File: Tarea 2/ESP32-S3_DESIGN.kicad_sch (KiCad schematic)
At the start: 31 parts, among them U1 ESP32-S3, U2 W25Q128JVS, U3 ESP-PSRAM32, U4 AMS1117-3.3, Y1 Crystal_Small

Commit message: Diseño de ESP32-S3 en KiCAD
Esta es la primera fase del diseño de una ESP32-S3, Aquí estamos realizando los esquematicos para la placa que vamos a desarrollar.
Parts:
- added C19: 0.1uF, symbol Device:C_Small
- added L8: TBD, symbol Device:L_Small
- added R3, R4, R6, R7, R8: 0, symbol Device:R_Small_US
- C7: value 0.1uF -> 1uF
- R2: value R_Small_US -> 499
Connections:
- net GND: now also U1.57 (GND), C19.2
- net LNA_IN: now also U1.1 (LNA_IN/RF)
- net SPICLK: now also R6.1
- net SPICS0: now also U1.32 (SPICS0/GPIO29)
- net SPID: now also R8.1
- net SPIHD: now also R3.1
- net SPIQ: now also R7.1
- net SPIWP: now also R4.1
- net VDD: now also U1.55 (VDDA), U1.56 (VDDA)
- net VDD_SPI: now also U1.29 (VDD_SPI)
- net XTAL_N: now also U1.53 (XTAL_N)
- net XTAL_P: now also L8.1
- net at C18.1: now also U1.20 (VDD3P3_RTC)
- net at R2.1: now also U1.49 (U0TXD/PROG/GPIO43)
- net U0TXD: now reaches R2.2
- net GPIO5: now reaches U1.10 (GPIO5/ADC1_CH4)
- net GPIO6: now reaches U1.11 (GPIO6/ADC1_CH5)
- net GPIO7: now reaches U1.12 (GPIO7/ADC1_CH6)
- net GPIO8: now reaches U1.13 (GPIO8/ADC1_CH7)
- net GPIO9: now reaches U1.14 (GPIO9/ADC1_CH8)
- net GPIO10: now reaches U1.15 (GPIO10/ADC1_CH9)
- net GPIO11: now reaches U1.16 (GPIO11/ADC2_CH0)
- net GPIO12: now reaches U1.17 (GPIO12/ADC2_CH1)
- net GPIO13: now reaches U1.18 (GPIO13/ADC2_CH2)
- net GPIO14: now reaches U1.19 (GPIO14/ADC2_CH3)
- net GPIO19: now reaches U1.25 (GPIO19/USB_D-/ADC2_CH8)
- net GPIO20: now reaches U1.26 (GPIO20/USB_D+/ADC2_CH9)
- net SPICS1 - GPIO26: now reaches U1.28 (SPI_CS1/GPIO26)
- net at U1.30 (SPIHD/GPIO27): now also R3.2
- net at U1.31 (SPIWP/GPIO28): now also R4.2
- net at U1.33 (SPICLK/GPIO30): now also R6.2
- net at U1.34 (SPIQ/GPIO31): now also R7.2
- net at U1.35 (SPID/GPIO32): now also R8.2
- net GPIO33: now reaches U1.38 (GPIO33)
- net GPIO34: now reaches U1.39 (GPIO34)
- net CHIP_PU: now reaches U1.4 (CHIP_PU/RESET)
- net GPIO35: now reaches U1.40 (GPIO35)
- net GPIO36: now reaches U1.41 (GPIO36)
- net GPIO37: now reaches U1.42 (GPIO37)
- net GPIO39: now reaches U1.44 (MTCK/JTAG/GPIO39)
- net GPIO40: now reaches U1.45 (MTDO/JTAG/GPIO40)
- net at U1.46 (VDD3P3_CPU): now also C19.1
- net GPIO41: now reaches U1.47 (MTDI/JTAG/GPIO41)
- net GPIO42: now reaches U1.48 (MTMS/JTAG/GPIO42)
- net GPIO0: now reaches U1.5 (GPIO0/BOOT)
- net U0RXD: now reaches U1.50 (U0RXD/PROG/GPIO44)
- net at U1.54 (XTAL_P): now also L8.2
- net GPIO1: now reaches U1.6 (GPIO1/ADC1_CH0)
- net GPIO2: now reaches U1.7 (GPIO2/ADC1_CH1)
- net GPIO3: now reaches U1.8 (GPIO3/ADC1_CH2)
- net GPIO4: now reaches U1.9 (GPIO4/ADC1_CH3)
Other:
- moved on the sheet: C12, C15, C16, C17, C18, L7, U1

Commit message: Diseño de ESP32-S3 en KiCAD
Esta es la primera fase del diseño de una ESP32-S3, Aquí estamos realizando los esquematicos para la placa que vamos a desarrollar.
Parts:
- removed C1: 10uF, symbol Device:C_Small
- removed D1: ESD, symbol Device:D_Small
- added C12: 10uF, symbol Device:C_Small
- added C20, C21: 0.1uF, symbol Device:C_Small
- added D2: ESD, symbol Device:D_Small
- added J1: USB_C_Receptacle_USB2.0_14P, symbol Connector:USB_C_Receptacle_USB2.0_14P
- added R7, R8: 5.1k, symbol Device:R_Small_US
- added U5: CH340C, Package_SO:SOIC-16_3.9x9.9mm_P1.27mm, symbol Interface_USB:CH340C
- renumbered C2 to C1, C11 to C10, C16 to C11, C17 to C13, C6 to C14, C7 to C15, C18 to C16, C19 to C17, C14 to C18, C13 to C19, C4 to C2, C8 to C3, C5 to C4, C9 to C5, C3 to C6, C10 to C7, C12 to C8, C15 to C9, D2 to D1, L4 to L1, L5 to L2, L6 to L3, L7 to L4, L8 to L5, R3 to R1, R4 to R2, R6 to R3, R7 to R4, R8 to R5, R2 to R6, U4 to U1, U1 to U4
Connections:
- net GND: now also C12.2, C20.1, C21.1, D2.1 (K), J1.A1 (GND), J1.A12 (GND), J1.B1 (GND), J1.B12 (GND), J1.SH (SHIELD), R7.2, R8.2, U5.1 (GND)
- net U0RXD: now also U5.2 (TXD)
- net U0TXD: now also U5.3 (RXD)
- net VBUS: now also C12.1, D2.2 (A), J1.A4 (VBUS), J1.A9 (VBUS), J1.B4 (VBUS), J1.B9 (VBUS)
- net VDD: now also C20.2, C21.2, U5.16 (VCC), U5.4 (V3)
- new net: J1.B5 (CC2), R8.1
- new net: J1.A5 (CC1), R7.1
- new net D+: J1.A6 (D+), J1.B6 (D+), U5.5 (UD+)
- new net D-: J1.A7 (D-), J1.B7 (D-), U5.6 (UD-)
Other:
- moved on the sheet: AE1, C1, C10, C11, C13, C16, C17, C18, C19, C2, C3, C4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

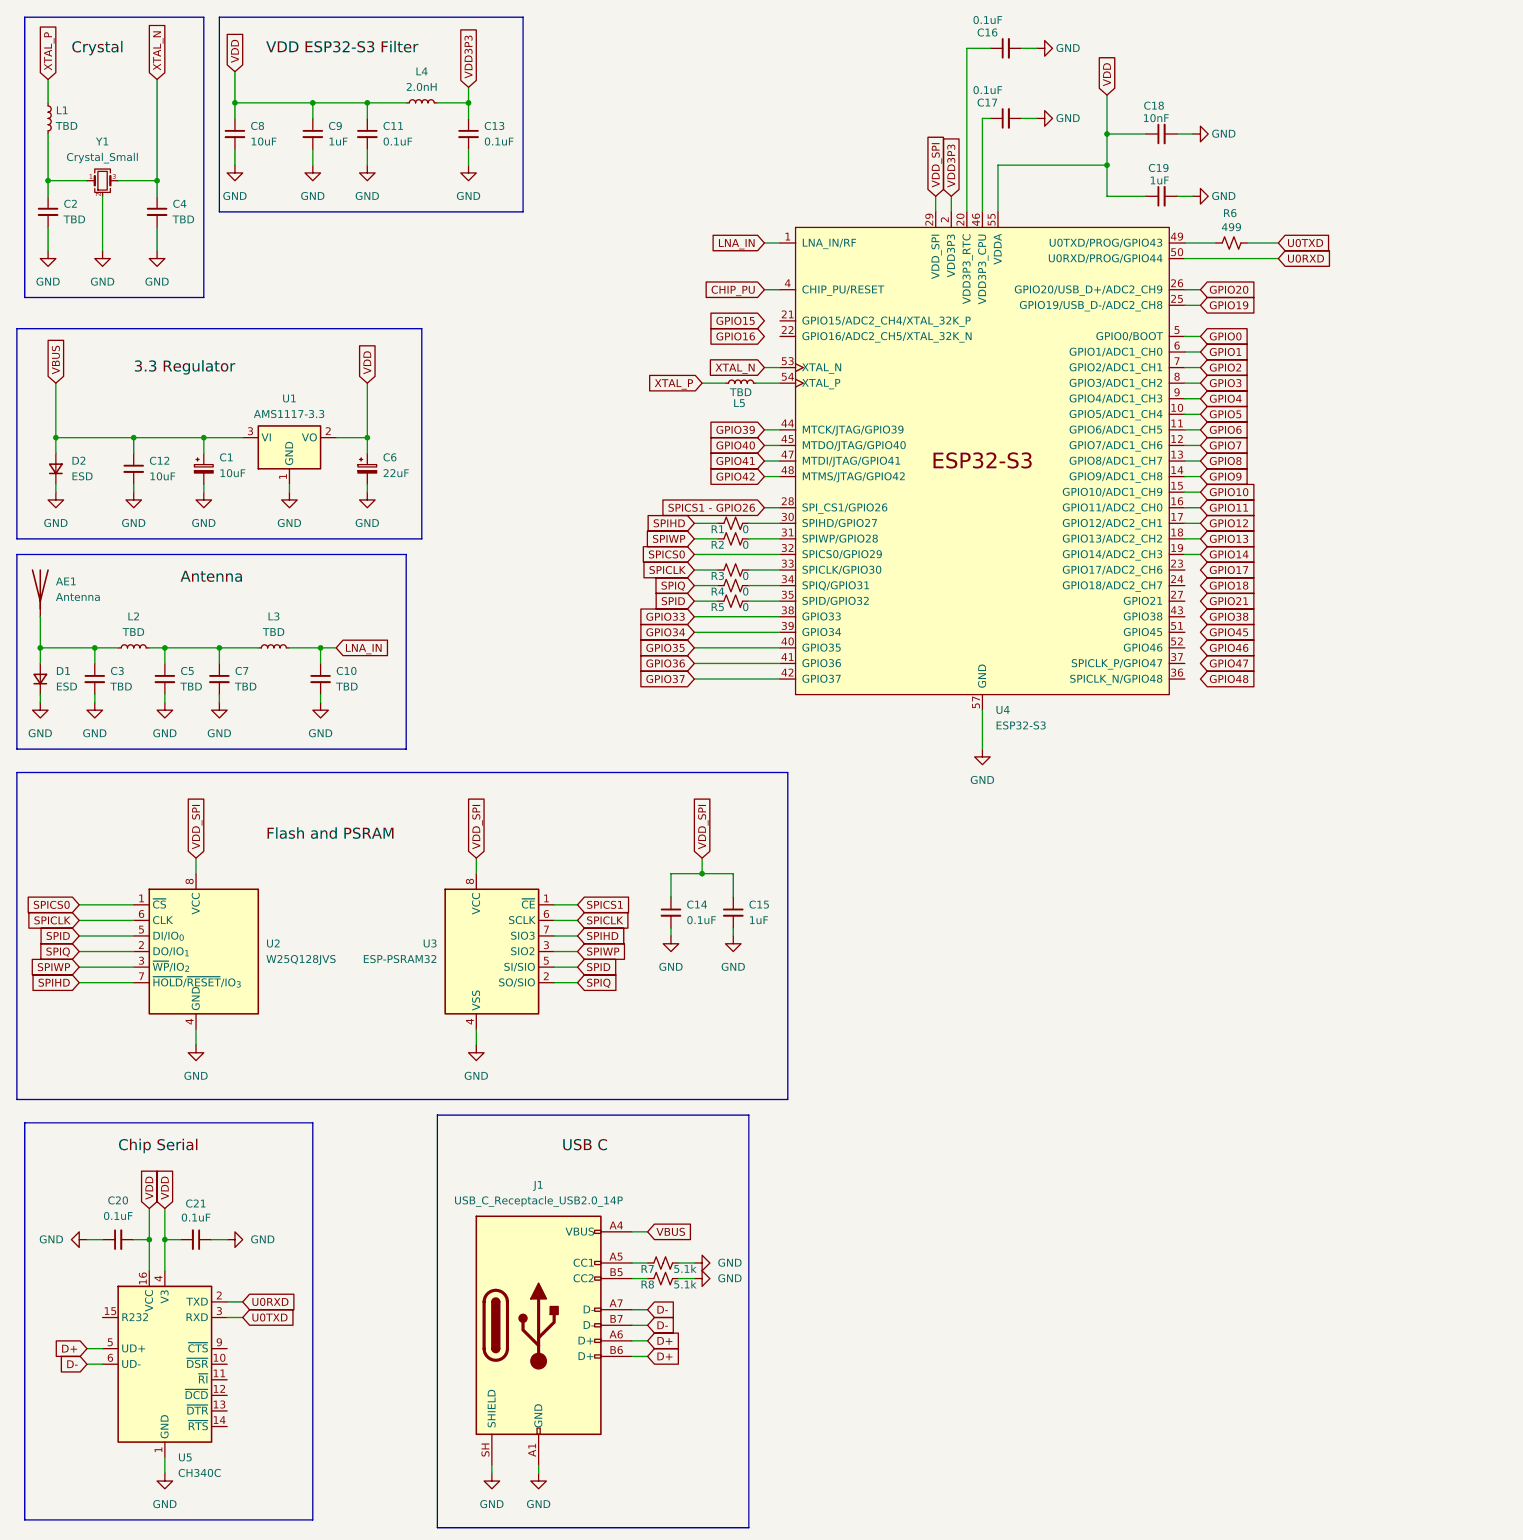
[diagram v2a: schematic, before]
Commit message: Diseño de ESP32-S3 en KiCAD
Esta es la primera fase del diseño de una ESP32-S3, Aquí estamos realizando los esquematicos de la parte del esp32 para la placa que vamos a desarrollar.
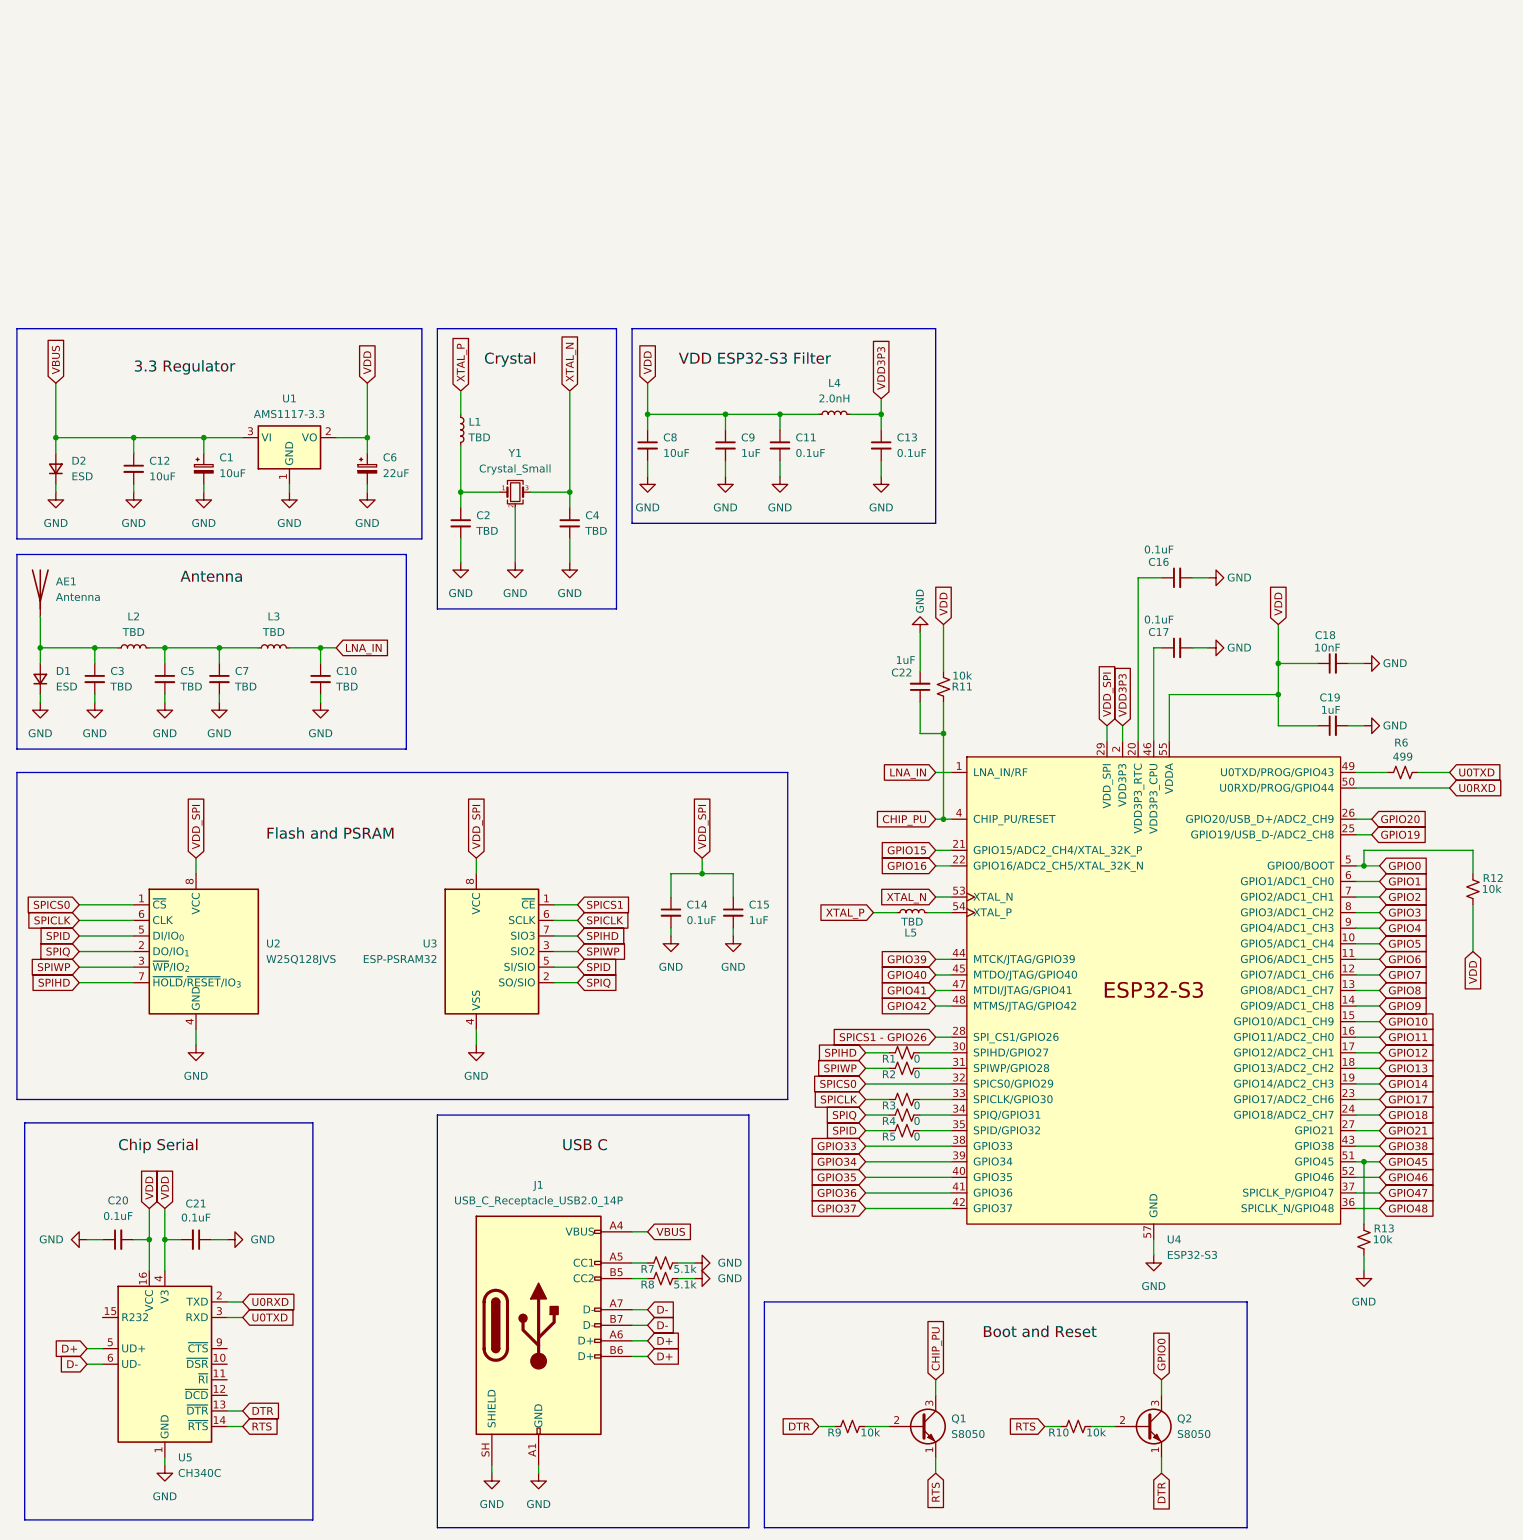
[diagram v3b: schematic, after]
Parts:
- added C22: 1uF, symbol Device:C_Small
- added Q1, Q2: S8050, Package_TO_SOT_THT:TO-92_Inline, symbol Transistor_BJT:S8050
- added R10, R11, R12, R13, R9: 10k, symbol Device:R_Small_US
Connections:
- net CHIP_PU: now also C22.1, Q1.3 (C), R11.1
- net GND: now also C22.2, R13.2
- net GPIO0: now also Q2.3 (C), R12.1
- net GPIO15: now also U4.21 (GPIO15/ADC2_CH4/XTAL_32K_P)
- net GPIO16: now also U4.22 (GPIO16/ADC2_CH5/XTAL_32K_N)
- net GPIO17: now also U4.23 (GPIO17/ADC2_CH6)
- net GPIO18: now also U4.24 (GPIO18/ADC2_CH7)
- net GPIO21: now also U4.27 (GPIO21)
- net GPIO38: now also U4.43 (GPIO38)
- net GPIO45: now also U4.51 (GPIO45), R13.1
- net GPIO46: now also U4.52 (GPIO46)
- net GPIO47: now also U4.37 (SPICLK_P/GPIO47)
- net GPIO48: now also U4.36 (SPICLK_N/GPIO48)
- net VDD: now also R11.2, R12.2
- net DTR: now reaches U5.13 (~{DTR})
- net DTR: now also Q2.1 (E), R9.1
- net RTS: now reaches U5.14 (~{RTS})
- net RTS: now also Q1.1 (E), R10.1
- new net: Q1.2 (B), R9.2
- new net: Q2.2 (B), R10.2
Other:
- moved on the sheet: C11, C13, C16, C17, C18, C19, C2, C4, C8, C9, L1, L4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

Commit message: Diseño de ESP32-S3 en KiCAD
Aquí están todos los esquemáticos que se utilizara para el desarrollo de nuestra placa de prueba de una esp32S3 con componentes agregados.
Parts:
- added BZ1: Buzzer, symbol Device:Buzzer
- added D3: LED_RGBK, symbol Device:LED_RGBK
- added D4: LED_A, symbol Device:LED
- added D5: LED_V, symbol Device:LED
- added D6: LED_R, symbol Device:LED
- added D7, D8: D_Small, symbol Device:D_Small
- added J2: Conn_01x22_Pin, symbol Connector:Conn_01x22_Pin
- added J3, J4: Screw_Terminal_01x03, symbol Connector:Screw_Terminal_01x03
- added K1: Relay_1, symbol Relay:Relay_SPDT
- added K2: Relay_2, symbol Relay:Relay_SPDT
- added Q3: RL_1, symbol Transistor_BJT:Q_NPN_BCE
- added Q4: RL_2, symbol Transistor_BJT:Q_NPN_BCE
- added Q5: BZ, symbol Transistor_BJT:Q_NPN_BCE
- added R14, R15, R16: 33, symbol Device:R_Small_US
- added R17, R18, R19: 330, symbol Device:R_Small_US
- added R20, R21, R25, R26, R27, R28: 10k, symbol Device:R_Small_US
- added R22, R23, R24: 1k, symbol Device:R_Small_US
- added RV1: Pot, symbol Device:R_Potentiometer_Small
- added SW1: B1, symbol Switch:SW_Push
- added SW2: B2, symbol Switch:SW_Push
- added SW3: Boot, symbol Switch:SW_Push
- added SW4: Reset, symbol Switch:SW_Push
- J1: value USB_C_Receptacle_USB2.0_14P -> USB_C
- Q1: value S8050 -> Reset
- Q2: value S8050 -> Boot
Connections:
- net CHIP_PU: now also R28.2, SW4.1
- net GND: now also D3.4 (K), D4.1 (K), D5.1 (K), D6.1 (K), Q3.3 (E), Q4.3 (E), Q5.3 (E), R26.2, RV1.3, SW1.2, SW2.2, SW3.2, SW4.2
- net GPIO0: now also R27.2, SW3.1
- net GPIO1: now also J2.1 (Pin_1)
- net GPIO10: now also J2.10 (Pin_10)
- net GPIO11: now also J2.11 (Pin_11)
- net GPIO12: now also J2.12 (Pin_12)
- net GPIO13: now also J2.13 (Pin_13)
- net GPIO14: now also J2.14 (Pin_14)
- net GPIO15: now also J2.16 (Pin_16)
- net GPIO16: now also J2.15 (Pin_15)
- net GPIO17: now also R25.2, R26.1, RV1.2
- net GPIO18: now also R24.1
- net GPIO19: now also J2.17 (Pin_17)
- net GPIO2: now also J2.2 (Pin_2)
- net GPIO20: now also J2.18 (Pin_18)
- net GPIO21: now also R21.2, SW2.1
- net GPIO3: now also J2.3 (Pin_3)
- net GPIO33: now also R16.2
- net GPIO34: now also R15.2
- net GPIO35: now also R14.2
- net GPIO36: now also R17.2
- net GPIO37: now also R18.2
- net GPIO38: now also R20.2, SW1.1
- net GPIO39: now also J2.19 (Pin_19)
- net GPIO4: now also J2.4 (Pin_4)
- net GPIO40: now also J2.20 (Pin_20)
- net GPIO41: now also J2.21 (Pin_21)
- net GPIO42: now also J2.22 (Pin_22)
- net GPIO46: now also R19.2
- net GPIO47: now also R22.1
- net GPIO48: now also R23.1
- net GPIO5: now also J2.5 (Pin_5)
- net GPIO6: now also J2.6 (Pin_6)
- net GPIO7: now also J2.7 (Pin_7)
- net GPIO8: now also J2.8 (Pin_8)
- net GPIO9: now also J2.9 (Pin_9)
- net VDD: now also BZ1.1 (+), D7.1 (K), D8.1 (K), K1.A1, K2.A1, R20.1, R21.1, R25.1, R27.1, R28.1, RV1.1
- new net: Q5.1 (B), R24.2
- new net: BZ1.2 (-), Q5.2 (C)
- new net: Q3.1 (B), R22.2
- new net: D7.2 (A), K1.A2, Q3.2 (C)
- new net: D5.2 (A), R18.1
- new net: D6.2 (A), R19.1
- new net: D8.2 (A), K2.A2, Q4.2 (C)
- new net: D3.3 (BA), R16.1
- new net: D4.2 (A), R17.1
- new net: Q4.1 (B), R23.2
- new net: D3.2 (GA), R15.1
- new net: D3.1 (RA), R14.1
- new net R1_C: J3.1 (Pin_1), K1.11
- new net R1_NA: J3.3 (Pin_3), K1.14
- new net R1_NC: J3.2 (Pin_2), K1.12
- new net R2_C: J4.1 (Pin_1), K2.11
- new net R2_NA: J4.3 (Pin_3), K2.14
- new net R2_NC: J4.2 (Pin_2), K2.12
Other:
- moved on the sheet: AE1, C1, C10, C11, C12, C13, C14, C15, C16, C17, C18, C19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
